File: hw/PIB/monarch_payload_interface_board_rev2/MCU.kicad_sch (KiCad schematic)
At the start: 21 parts, among them J16 20021121-00008C4LF, SW1 SW_Push, SW2 SW_Push, U2 STM32L4A6VGTx

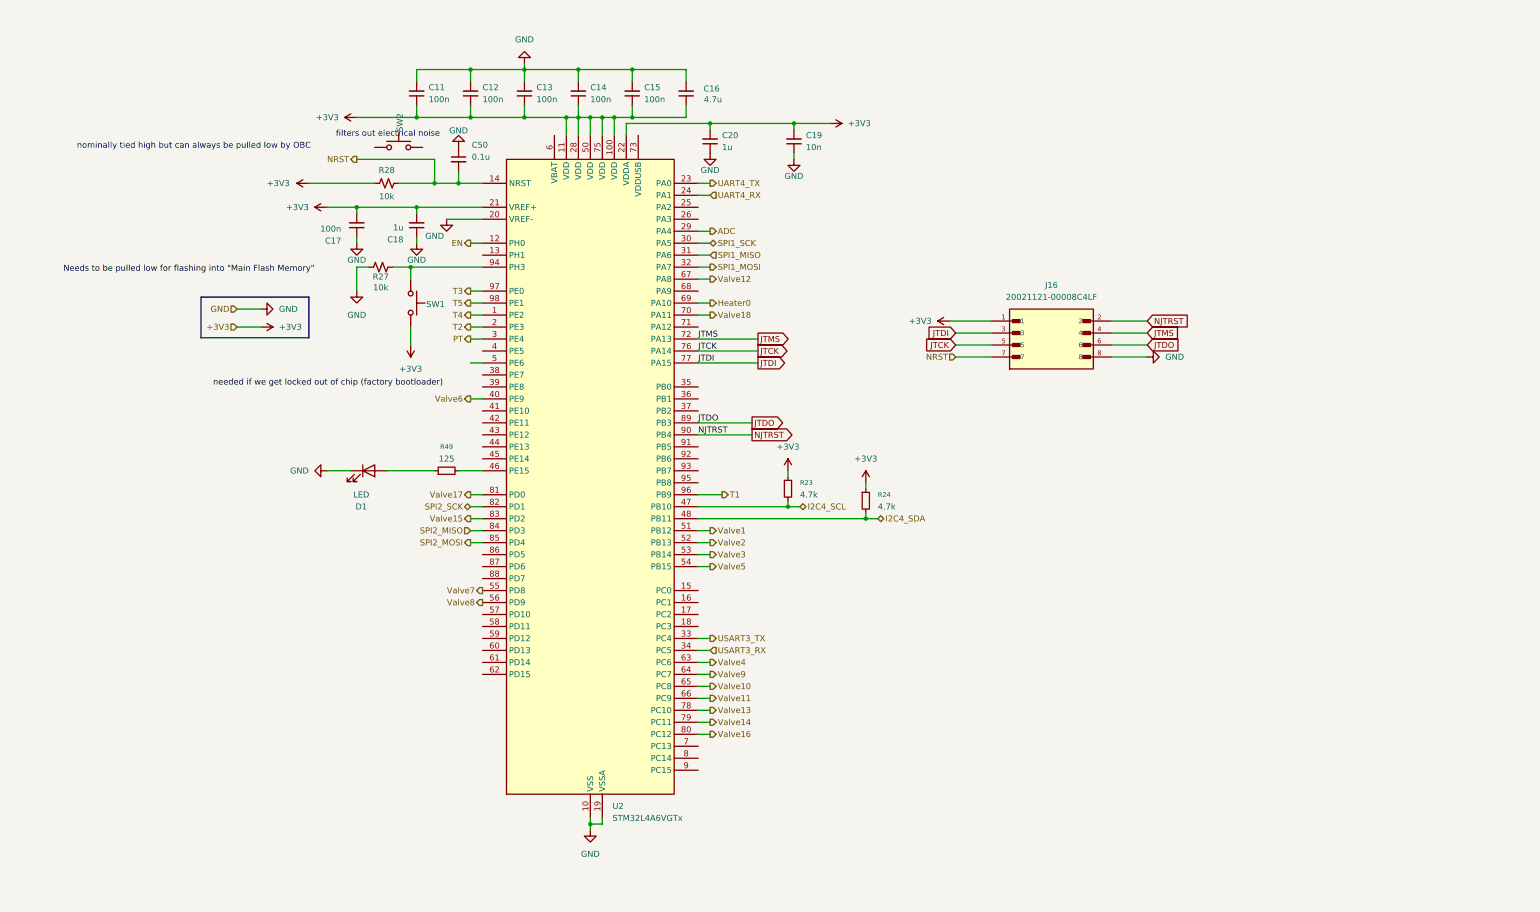
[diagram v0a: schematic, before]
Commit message: Debugging LEDS, Power LEDs, and Button for NRST
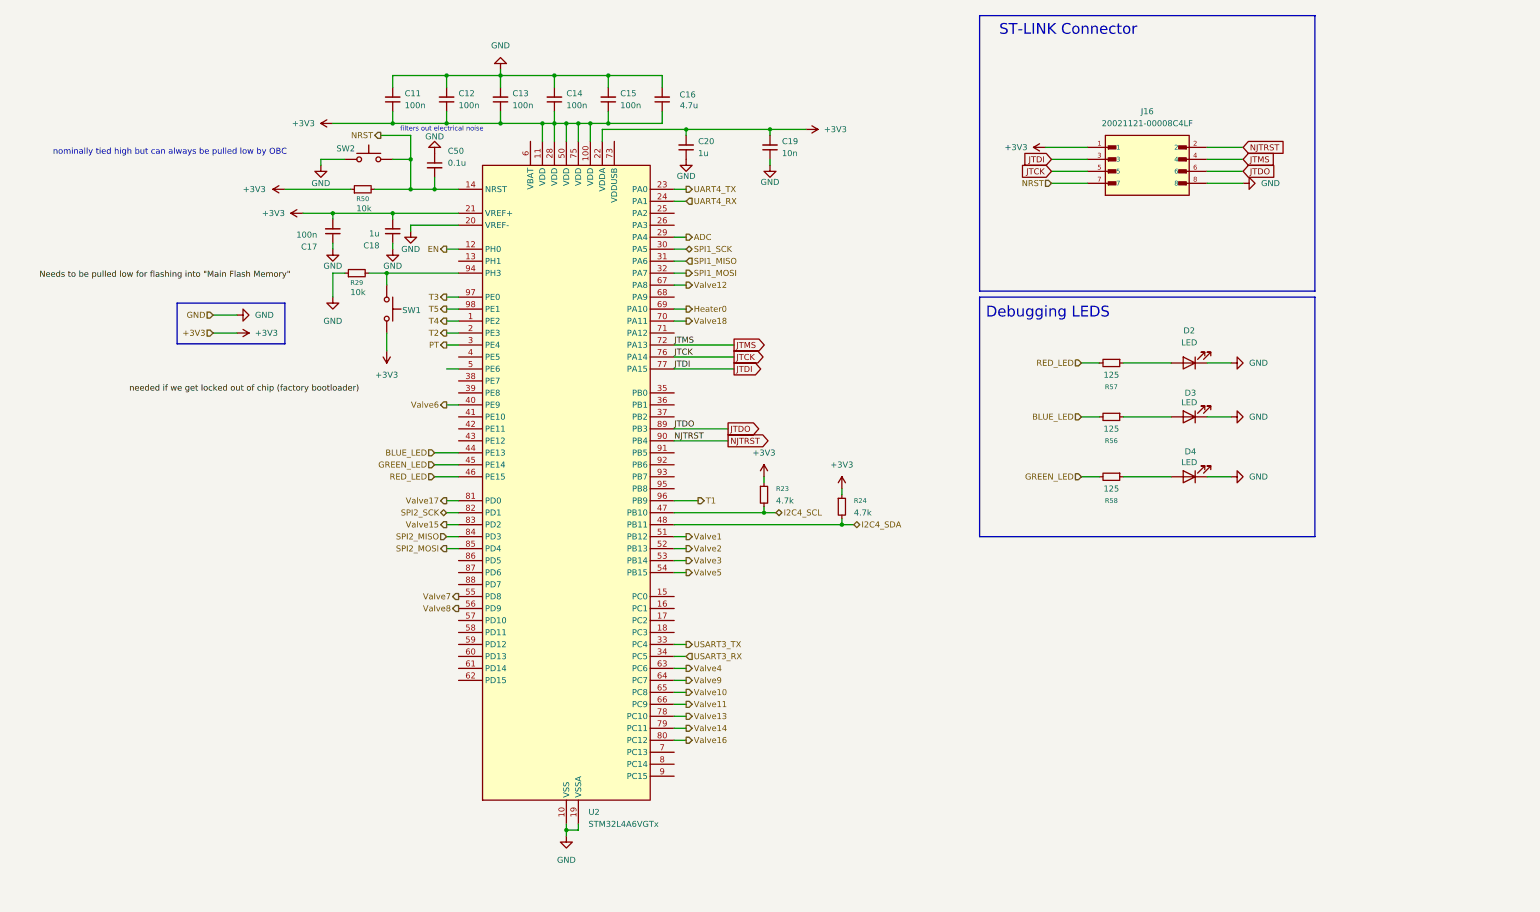
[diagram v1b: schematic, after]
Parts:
- removed D1: LED, LED_SMD:LED_0603_1608Metric, symbol Device:LED
- removed R27, R28: 10k, symbol Device:R_Small_US
- removed R49: 125, Resistor_SMD:R_0603_1608Metric, symbol Device:R_Small
- added D2, D3, D4: LED, LED_SMD:LED_0603_1608Metric, symbol Device:LED
- added R29, R50: 10k, Resistor_SMD:R_0603_1608Metric, symbol Device:R_Small
- added R56, R57, R58: 125, Resistor_SMD:R_0603_1608Metric, symbol Device:R_Small
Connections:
- net +3V3: now also R50.1
- net GND: now also SW2.1, D2.1 (K), D3.1 (K), D4.1 (K), R29.1
- net NRST: now also SW2.2, R50.2
- net at SW1.1, U2.94 (PH3): now also R29.2
- net BLUE_LED: now reaches U2.44 (PE13)
- net BLUE_LED: now also R56.2
- net GREEN_LED: now reaches U2.45 (PE14)
- net GREEN_LED: now also R58.2
- net RED_LED: now reaches U2.46 (PE15)
- net RED_LED: now also R57.2
- new net: D2.2 (A), R57.1
- new net: D4.2 (A), R58.1
- new net: D3.2 (A), R56.1
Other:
- note added: "Debugging LEDS"
- note added: "ST-LINK Connector"
- moved on the sheet: C11, C12, C13, C14, C15, C16, C17, C18, C19, C20, C50, J16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

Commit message: MCU Power Pins Fix
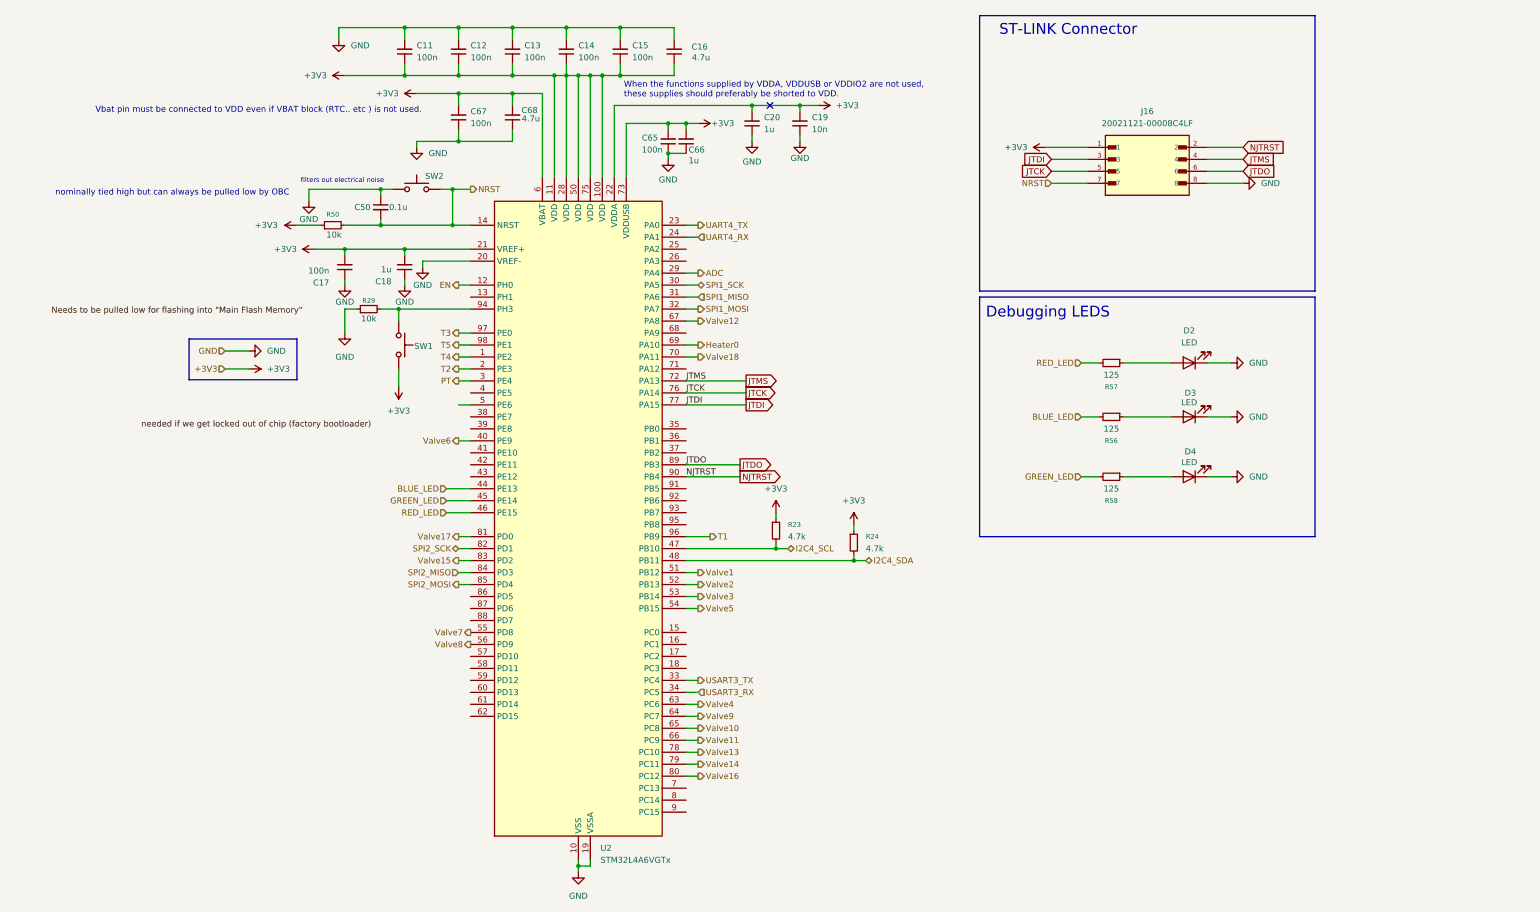
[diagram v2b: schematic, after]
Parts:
- added C65, C67: 100n, Capacitor_SMD:C_0603_1608Metric, symbol Device:C_Small
- added C66: 1u, Capacitor_SMD:C_0603_1608Metric, symbol Device:C_Small
- added C68: 4.7u, Capacitor_SMD:C_0603_1608Metric, symbol Device:C_Small
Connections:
- net +3V3: now also U2.6 (VBAT), U2.73 (VDDUSB), C65.2, C66.2, C67.2, C68.2
- net GND: now also C65.1, C66.1, C67.1, C68.1
- no-connect marks 0 -> 1
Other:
- note added: "Vbat pin must be connected to VDD even if VBAT block (RTC.. etc ) is not used."
- note added: "When the functions supplied by VDDA, VDDUSB or VDDIO2 are not used, these supplies should preferably be shorted to VDD."
- moved on the sheet: C11, C12, C13, C14, C15, C16, C17, C18, C19, C20, C50, R23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

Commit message: Connector Additions
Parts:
- added J17: Conn_02x04_Counter_Clockwise, symbol Connector_Generic:Conn_02x04_Counter_Clockwise
- SW1: value SW_Push -> SW_BOOT
- SW2: value SW_Push -> SW_RESET
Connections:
- net +3V3: now also J17.1 (Pin_1); no longer J16.1
- net GND: no longer J16.8
- net JTCK: now also J17.3 (Pin_3); no longer J16.5
- net JTDI: now also J17.2 (Pin_2); no longer J16.3
- net JTDO: no longer J16.6
- net JTMS: no longer J16.4
- net NJTRST: no longer J16.2
- net NRST: now also J17.4 (Pin_4); no longer J16.7
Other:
- note added: "STM32L4A6VG"
- moved on the sheet: C11, C12, C13, C14, C15, C16, C17, C18, C19, C20, C50, C65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

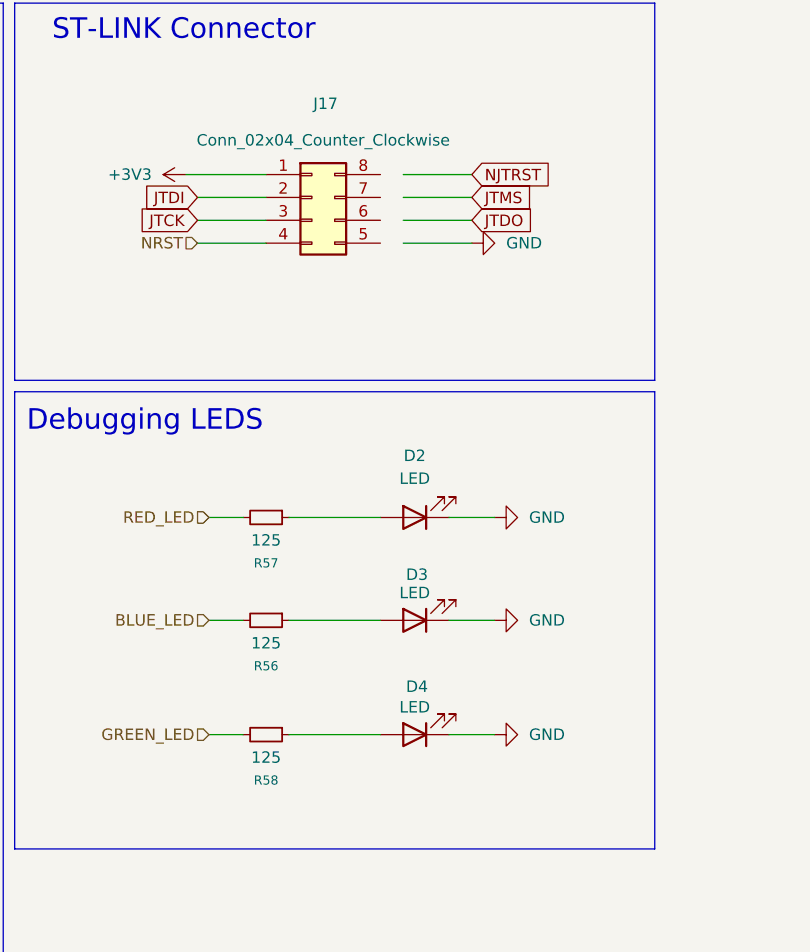
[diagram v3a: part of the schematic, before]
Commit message: LED 12 VOLT Values / New Connector Footprints added
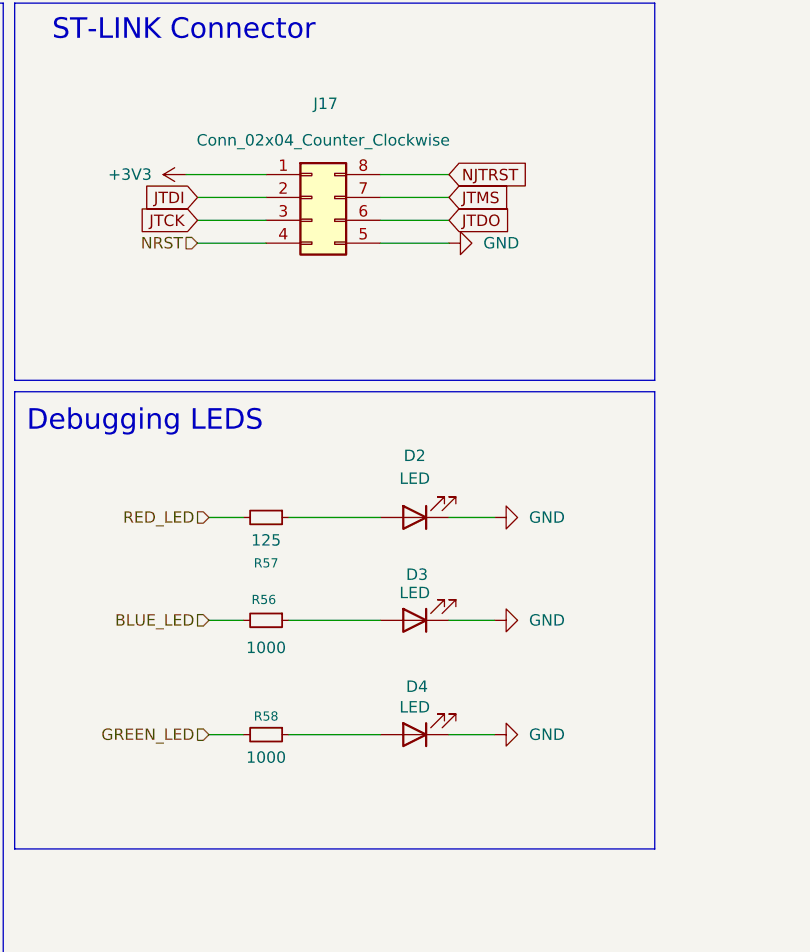
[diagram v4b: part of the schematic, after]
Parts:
- R56, R58: value 125 -> 1000
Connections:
- net GND: now also J17.5 (Pin_5)
- net JTDO: now also J17.6 (Pin_6)
- net JTMS: now also J17.7 (Pin_7)
- net NJTRST: now also J17.8 (Pin_8)
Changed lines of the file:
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@@
 	(wire
 		(pts
-			(xy 228.6 39.37) (xy 220.98 39.37)
+			(xy 226.06 39.37) (xy 218.44 39.37)
 		)
 		(stroke
@@
 	(wire
 		(pts
-			(xy 228.6 31.75) (xy 220.98 31.75)
+			(xy 226.06 31.75) (xy 218.44 31.75)
 		)
 		(stroke
@@
 	(wire
 		(pts
-			(xy 228.6 34.29) (xy 220.98 34.29)
+			(xy 226.06 34.29) (xy 218.44 34.29)
 		)
 		(stroke
@@
 	(wire
 		(pts
-			(xy 228.6 36.83) (xy 220.98 36.83)
+			(xy 226.06 36.83) (xy 218.44 36.83)
 		)
 		(stroke
@@
 	(global_label "JTMS"
 		(shape input)
-		(at 228.6 34.29 0)
+		(at 226.06 34.29 0)
 		(fields_autoplaced yes)
 		(effects
@@
 		)
 		(property "Intersheetrefs" "${INTERSHEET_REFS}"
-			(at 235.5271 34.29 0)
+			(at 232.9871 34.29 0)
 			(hide yes)
 			(show_name no)
@@
 	(global_label "NJTRST"
 		(shape input)
-		(at 228.6 31.75 0)
+		(at 226.06 31.75 0)
 		(fields_autoplaced yes)
 		(effects
@@
 		)
 		(property "Intersheetrefs" "${INTERSHEET_REFS}"
-			(at 237.6438 31.75 0)
+			(at 235.1038 31.75 0)
 			(hide yes)
 			(show_name no)
@@
 	(global_label "JTDO"
 		(shape input)
-		(at 228.6 36.83 0)
+		(at 226.06 36.83 0)
 		(fields_autoplaced yes)
 		(effects
@@
 		)
 		(property "Intersheetrefs" "${INTERSHEET_REFS}"
-			(at 235.4667 36.83 0)
+			(at 232.9267 36.83 0)
 			(hide yes)
 			(show_name no)
@@
 		(in_pos_files yes)
 		(dnp no)
-		(fields_autoplaced yes)
 		(property "Reference" "R58"
-			(at 205.74 99.06 90)
+			(at 205.74 91.948 90)
 			(show_name no)
 			(do_not_autoplace no)
@@
 			)
 		)
-		(property "Value" "125"
+		(property "Value" "1000"
 			(at 205.74 96.52 90)
 			(show_name no)
@@
 	(symbol
 		(lib_id "power:GND")
-		(at 228.6 39.37 90)
+		(at 226.06 39.37 90)
 		(unit 1)
 		(body_style 1)
@@
 		(fields_autoplaced yes)
 		(property "Reference" "#PWR028"
-			(at 234.95 39.37 0)
+			(at 232.41 39.37 0)
 			(hide yes)
 			(show_name no)
@@
 		)
 		(property "Value" "GND"
-			(at 232.41 39.3701 90)
+			(at 229.87 39.3701 90)
 			(show_name no)
 			(do_not_autoplace no)
@@
 		)
 		(property "Footprint" ""
-			(at 228.6 39.37 0)
+			(at 226.06 39.37 0)
 			(hide yes)
 			(show_name no)
@@
 		)
 		(property "Datasheet" ""
-			(at 228.6 39.37 0)
+			(at 226.06 39.37 0)
 			(hide yes)
 			(show_name no)
@@
 		)
 		(property "Description" "Power symbol creates a global label with name \"GND\" , ground"
-			(at 228.6 39.37 0)
+			(at 226.06 39.37 0)
 			(hide yes)
 			(show_name no)
@@
 		(in_pos_files yes)
 		(dnp no)
-		(fields_autoplaced yes)
 		(property "Reference" "R56"
-			(at 205.74 86.36 90)
+			(at 205.486 78.994 90)
 			(show_name no)
 			(do_not_autoplace no)
@@
 			)
 		)
-		(property "Value" "125"
-			(at 205.74 83.82 90)
+		(property "Value" "1000"
+			(at 205.74 84.328 90)
 			(show_name no)
 			(do_not_autoplace no)
